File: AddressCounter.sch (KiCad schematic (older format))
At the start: 13 parts, among them U13 SN74LV163A, U14 SN74LV163A, U16 SN74LV163A, U17 SN74LV163A, U18 74AHC1G04, U19 SN74LV163A, U20 SN74LV163A

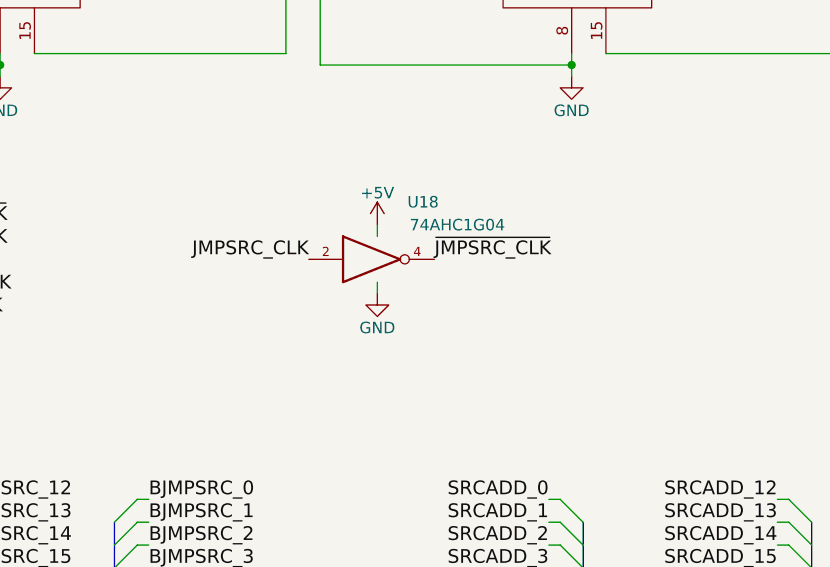
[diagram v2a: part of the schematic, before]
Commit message: Multiple change : Replacing old custom "LTC6994-1" symbol with the Kicad symbol "LTC6994xS6-1" Replacing old custom "LM810" symbol with the Kicad symbol "LM810" Replacing all hidden power pins symbols (hidden pins bug) Renaming "Main connector" to "SPS1 Processor connector" Removing old symbols, cleaning Replacing symbol "CD74AC238" with a new one
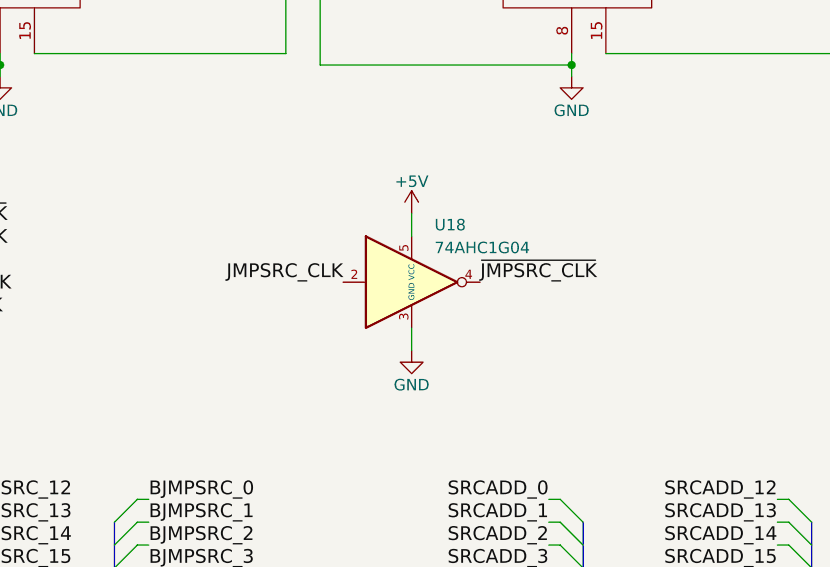
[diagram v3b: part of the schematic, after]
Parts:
- removed U18: 74AHC1G04, Package_TO_SOT_SMD:SOT-23-5, symbol 74xGxx:74AHC1G04
- added U18: 74AHC1G04, symbol Custom:74AHC1G04
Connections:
- net +5V: now also U18.5 (VCC)
- net GND: now also U18.3 (GND)
- net JMPSRC_CLK: now also U18.2
- net ~JMPSRC_CLK: now also U18.4
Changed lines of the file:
@@
 L power:GND #PWR083
 U 1 1 5BB5F937
-P 3550 5100
+P 3700 5350
 AR Path="/5BB5F937" Ref="#PWR083"  Part="1"
 AR Path="/5A93FC93/5BB5F937" Ref="#PWR083"  Part="1"
-F 0 "#PWR083" H 3550 4850 50  0001 C CNN
-F 1 "GND" H 3550 4950 50  0000 C CNN
-F 2 "" H 3550 5100 50  0001 C CNN
-F 3 "" H 3550 5100 50  0001 C CNN
-	1    3550 5100
+F 0 "#PWR083" H 3700 5100 50  0001 C CNN
+F 1 "GND" H 3700 5200 50  0000 C CNN
+F 2 "" H 3700 5350 50  0001 C CNN
+F 3 "" H 3700 5350 50  0001 C CNN
+	1    3700 5350
 	1    0    0    -1
 $EndComp
@@
 L power:+5V #PWR084
 U 1 1 5BB5F9A2
-P 3550 4800
+P 3700 4750
 AR Path="/5BB5F9A2" Ref="#PWR084"  Part="1"
 AR Path="/5A93FC93/5BB5F9A2" Ref="#PWR084"  Part="1"
-F 0 "#PWR084" H 3550 4650 50  0001 C CNN
-F 1 "+5V" H 3550 4940 50  0000 C CNN
-F 2 "" H 3550 4800 50  0001 C CNN
-F 3 "" H 3550 4800 50  0001 C CNN
-	1    3550 4800
-	1    0    0    -1
-$EndComp
-Text Label 3250 4950 2    60   ~ 0
+F 0 "#PWR084" H 3700 4600 50  0001 C CNN
+F 1 "+5V" H 3700 4890 50  0000 C CNN
+F 2 "" H 3700 4750 50  0001 C CNN
+F 3 "" H 3700 4750 50  0001 C CNN
+	1    3700 4750
+	1    0    0    -1
+$EndComp
+Text Label 3400 5050 2    60   ~ 0
 JMPSRC_CLK
-Text Label 3800 4950 0    60   ~ 0
-~JMPSRC_CLK
-Wire Wire Line
-	3550 4850 3550 4800
-Wire Wire Line
-	3550 5050 3550 5100
+Text Label 4000 5050 0    60   ~ 0
+~JMPSRC_CLK
 Text Label 1400 4800 0    60   ~ 0
 ~GLOBAL_CLK
@@
 Wire Wire Line
 	7050 4100 7050 4150
-$Comp
-L 74xGxx:74AHC1G04 U18
-U 1 1 5D17D605
-P 3550 4950
-F 0 "U18" H 3750 5200 50  0000 C CNN
-F 1 "74AHC1G04" H 3900 5100 50  0000 C CNN
-F 2 "Package_TO_SOT_SMD:SOT-23-5" H 3550 4950 50  0001 C CNN
-F 3 "http://www.ti.com/lit/sg/scyt129e/scyt129e.pdf" H 3550 4950 50  0001 C CNN
-	1    3550 4950
-	1    0    0    -1
-$EndComp
 $Comp
 L Custom:SN74LV163A U19
@@
 Text Label 6550 1350 2    60   ~ 0
 ~GLOBAL_CLK
+$Comp
+L Custom:74AHC1G04 U?
+U 1 1 5F9095CA
+P 3700 5050
+AR Path="/5F9095CA" Ref="U?"  Part="1"
+AR Path="/5A93FC93/5F9095CA" Ref="U18"  Part="1"
+F 0 "U18" H 3800 5300 50  0000 L CNN
+F 1 "74AHC1G04" H 3800 5200 50  0000 L CNN
+F 2 "" H 3700 5050 50  0001 C CNN
+F 3 "https://assets.nexperia.com/documents/data-sheet/74AHC_AHCT1G04.pdf" H 3700 5050 50  0001 C CNN
+	1    3700 5050
+	1    0    0    -1
+$EndComp
+Wire Wire Line
+	3700 5350 3700 5250
+Wire Wire Line
+	3700 4850 3700 4750
 Wire Bus Line
 	5450 6100 5450 7300
